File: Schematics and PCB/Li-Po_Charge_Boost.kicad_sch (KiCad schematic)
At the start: 23 parts, among them Q1 FS8205, SW107 SPDT, U7 TP4056, U8 MT3608, U9 FS312F-G

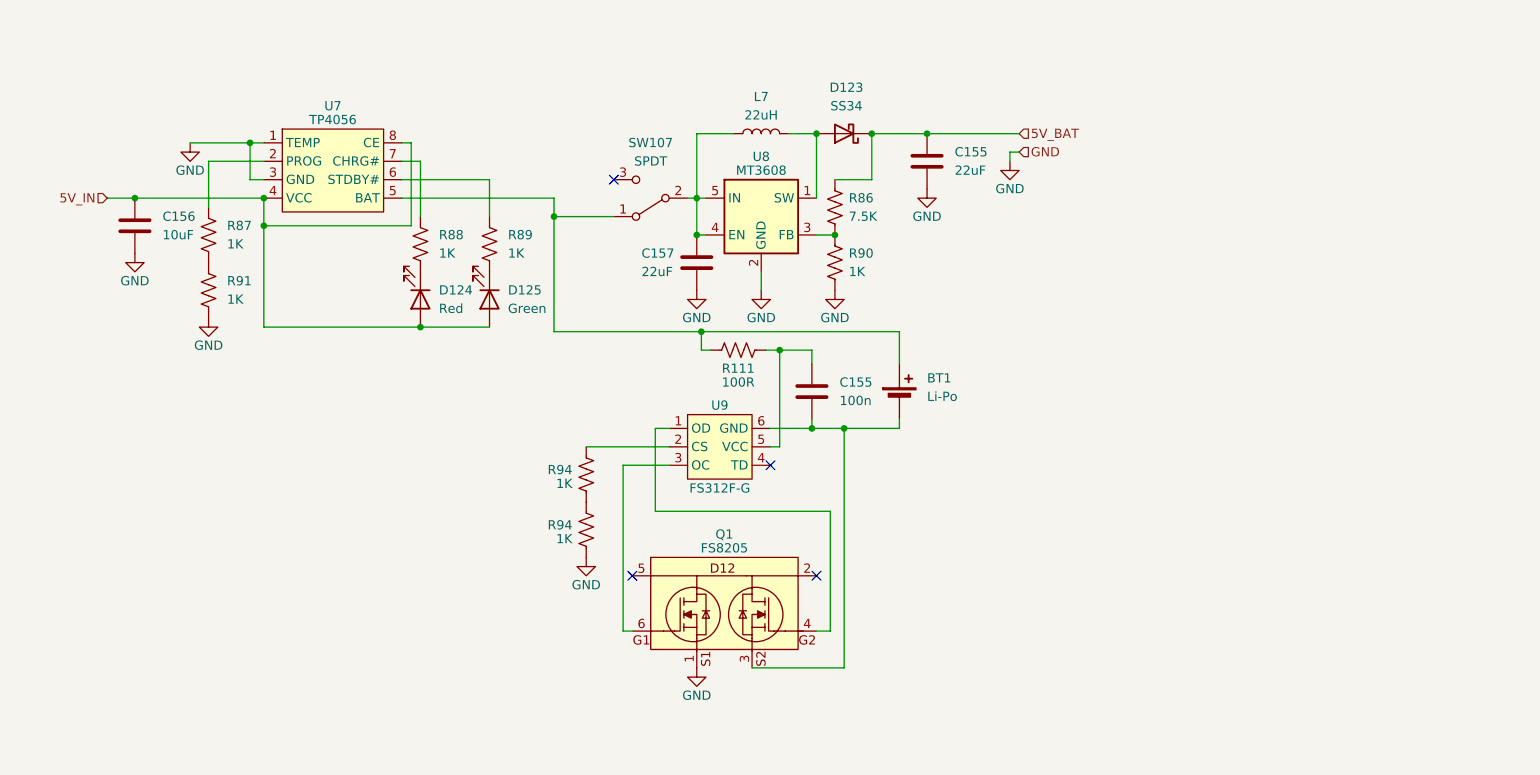
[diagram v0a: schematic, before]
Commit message: Updated USB hub
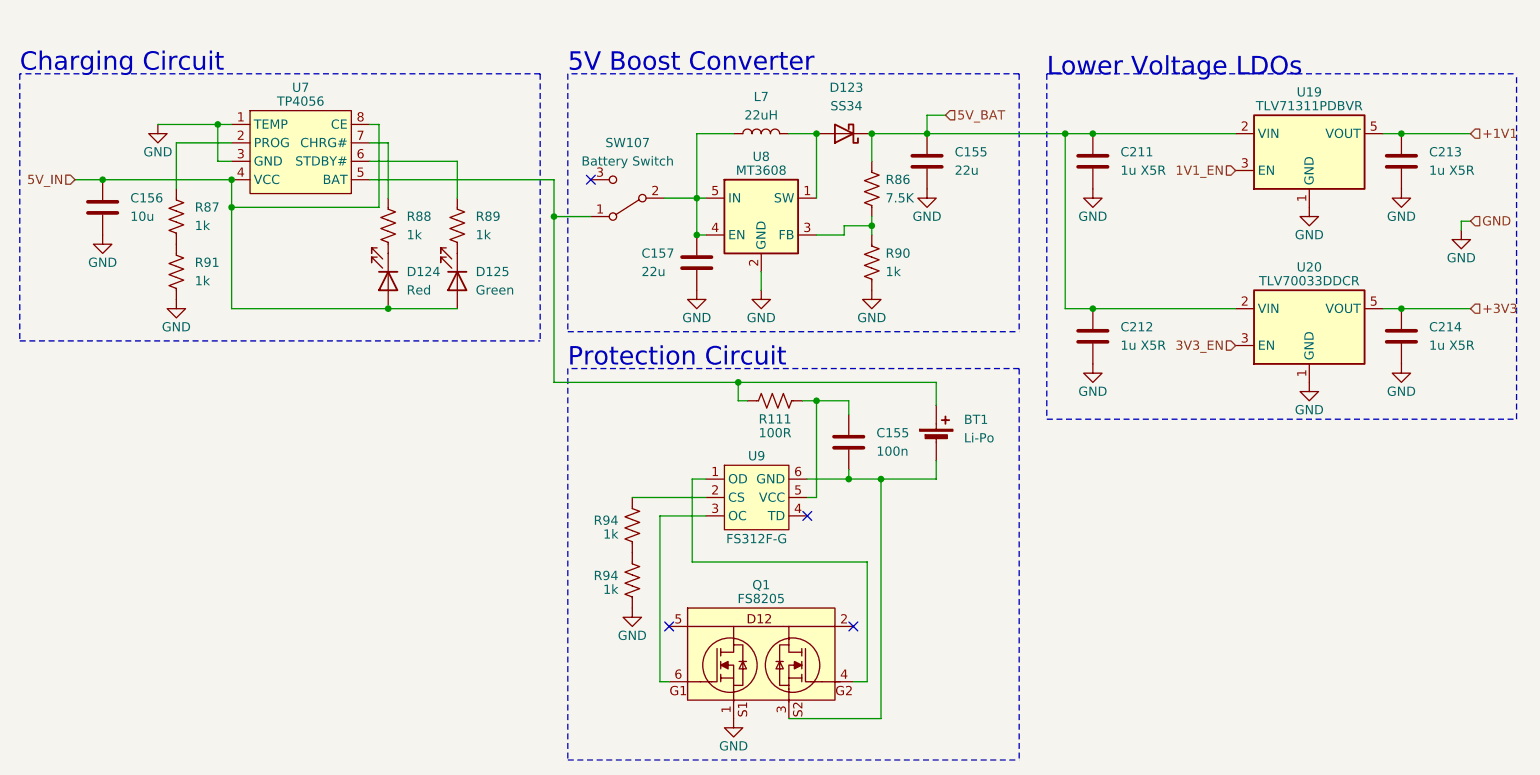
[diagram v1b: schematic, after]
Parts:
- added C211, C212, C213, C214: 1u X5R, symbol Device:C
- added U19: TLV71311PDBVR, Package_TO_SOT_SMD:TSOT-23-5, symbol Regulator_Linear:ADP7182AUJZ-1.8
- added U20: TLV70033DDCR, Package_TO_SOT_SMD:TSOT-23-5, symbol Regulator_Linear:ADP7182AUJZ-1.8
- C155, C157: value 22uF -> 22u
- C156: value 10uF -> 10u
- R87, R88, R89, R90, R91, R94: value 1K -> 1k
- SW107: value SPDT -> Battery Switch
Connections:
- net 5V_BAT: now also C211.1, C212.1, U19.2 (VIN), U20.2 (VIN)
- net GND: now also C211.2, C212.2, C213.2, C214.2, U19.1 (GND), U20.1 (GND)
- new net +1V1: C213.1, U19.5 (VOUT)
- new net +3V3: C214.1, U20.5 (VOUT)
- new net 1V1_EN: U19.3 (EN)
- new net 3V3_EN: U20.3 (EN)
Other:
- note added: "5V Boost Converter"
- note added: "Charging Circuit"
- note added: "Lower Voltage LDOs"
- note added: "Protection Circuit"
- moved on the sheet: BT1, C155, C156, D124, D125, Q1, R111, R86, R87, R88, R89, R90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

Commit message: minor changes
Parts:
- removed BT1: Li-Po, symbol Device:Battery_Cell
- removed C155, C157: 22u, Capacitor_SMD:C_0603_1608Metric, symbol Device:C
- removed C155: 100n, Capacitor_SMD:C_0603_1608Metric, symbol Device:C
- removed C156: 10u, Capacitor_SMD:C_0603_1608Metric, symbol Device:C
- removed D124: Red, LED_SMD:LED_0805_2012Metric, symbol Device:LED
- removed D125: Green, LED_SMD:LED_0805_2012Metric, symbol Device:LED
- removed Q1: FS8205, Package_TO_SOT_SMD:SOT-23-6, symbol Li-Ion Charge Boost Protect:FS8205
- removed R111: 100R, symbol Device:R_US
- removed R87, R88, R89, R91, R94 (x2): 1k, Resistor_SMD:R_0603_1608Metric, symbol Device:R_US
- removed SW107: Battery Switch, Connector_PinHeader_2.54mm:PinHeader_1x03_P2.54mm_Vertical, symbol Switch:SW_SPDT
- removed U7: TP4056, Package_SO:SOP-8-1EP_4.57x4.57mm_P1.27mm_EP4.57x4.45mm_ThermalVias, symbol Li-Ion Charge Boost Protect:TP4056
- removed U8: MT3608, Package_TO_SOT_SMD:SOT-23-6, symbol Regulator_Switching:MT3608
- removed U9: FS312F-G, Package_TO_SOT_SMD:SOT-23-6, symbol Li-Ion Charge Boost Protect:FS312F-G
- added BT2: Li-Po, symbol Device:Battery_Cell
- added C210, C211: 22u, symbol Device:C
- added C243: 100n, Capacitor_SMD:C_0603_1608Metric, symbol Device:C
- added D131: RED, LED_SMD:LED_0805_2012Metric, symbol Device:LED
- added D132: GREEN, LED_SMD:LED_0805_2012Metric, symbol Device:LED
- added Q1: FS8205, Package_TO_SOT_SMD:SOT-23-6, symbol Transistor_FET:DMG9926UDM
- added R114, R115, R116, R117: 1k, Resistor_SMD:R_0603_1608Metric, symbol Device:R_US
- added R118, R119: 330R, Resistor_SMD:R_0603_1608Metric, symbol Device:R_US
- added U1: TP4056-42-ESOP8, Package_SO:SOIC-8-1EP_3.9x4.9mm_P1.27mm_EP2.41x3.3mm_ThermalVias, symbol Battery_Management:TP4056-42-ESOP8
- added U2: MT3608, Package_TO_SOT_SMD:SOT-23-6, symbol Regulator_Switching:MT3608
- added U3: AP9101CK, Package_TO_SOT_SMD:SOT-23-5, symbol Battery_Management:AP9101CK
- R105: renamed from R86; value 7.5K -> 75k
- R109: renamed from R90; value 1k -> 10k
- renumbered C211 to C208, C213 to C209, C214 to C213, D123 to D128, L7 to L1, U19 to U21, U20 to U23
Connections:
- net 3V3_EN is gone; now on net +5V: U23.3 (EN)
- net 5V_BAT is gone; now on net +5V: C208.1, C212.1, D128.1 (K), R105.1, U21.2 (VIN), U23.2 (VIN)
- net GND: now also C210.2, C211.2, Q1.1 (D1), R117.2, R119.2, U1.1 (TEMP), U1.3 (GND), U1.9 (EPAD), U2.2 (GND)
- net at R105.2, R109.1: now also U2.3 (FB)
- net at D128.2 (A), L1.2: now also U2.1 (SW)
- net at L1.1: now also BT2.1 (+), C210.1, C243.2, R118.1, U1.5 (BAT), U2.4 (EN), U2.5 (IN)
- net 1V1_EN renamed +5V
- net +5V: now also C211.1
- new net: R114.1, U1.7 (~{CHRG})
- new net: D131.1 (K), R114.2
- new net: R116.1, U1.2 (PROG)
- new net: R115.1, U1.6 (~{STDBY})
- new net: R118.2, U3.2 (VDD)
- new net: BT2.2 (-), C243.1, Q1.3 (S2), U3.3 (VSS)
- new net: D132.1 (K), R115.2
- new net: R116.2, R117.1
- new net: Q1.2 (S1/D2), Q1.5 (S1/D2)
- new net: Q1.4 (G2), U3.4 (DO)
- new net: Q1.6 (G1), U3.5 (CO)
- new net: R119.1, U3.1 (VM)
- new net 5V_USB: D131.2 (A), D132.2 (A), U1.4 (V_{CC}), U1.8 (CE)
- no-connect marks 4 -> 1
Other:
- note added: "Battery charging"
- note removed: "Charging Circuit"
- moved on the sheet: C208, C209, C212, C213, D128, L1, R105, R109, U21, U23

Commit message: layout improvements
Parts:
- removed C208, C209, C212, C213: 1u X5R, symbol Device:C
- removed U21: TLV71311PDBVR, Package_TO_SOT_SMD:TSOT-23-5, symbol Regulator_Linear:ADP7182AUJZ-1.8
- removed U23: TLV70033DDCR, Package_TO_SOT_SMD:TSOT-23-5, symbol Regulator_Linear:ADP7182AUJZ-1.8
- BT1: renamed from BT2; footprint (none) -> Connector_PinHeader_2.54mm:PinHeader_1x02_P2.54mm_Vertical
- C1: renamed from C210; footprint (none) -> Capacitor_SMD:C_0603_1608Metric
- C2: renamed from C211; footprint (none) -> Capacitor_SMD:C_0603_1608Metric
- renumbered C243 to C7, D132 to D1, D131 to D2, D128 to D3, R118 to R10, R119 to R11, R115 to R4, R114 to R5, R105 to R6, R116 to R7, R109 to R8, R117 to R9, U1 to U2, U2 to U3, U3 to U5
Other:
- note removed: "Lower Voltage LDOs"
- moved on the sheet: BT1, C7, D1, D2, Q1, R10, R11, R4, R5, R7, R9, U2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
